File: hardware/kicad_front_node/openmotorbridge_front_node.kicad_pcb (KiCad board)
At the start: 2 copper layers, 68 x 44 mm, 32 parts, among them J1 12V_KL30_KL15_GND, J2 CAN_H_L_GND, J3 PTT_IN_GND, J4 USB_UPSTREAM_HOST, J5 USB_DN1_GLOVEBOX, J6 USB_DN2_CARPLAY, J7 USB-C_SERVICE, SW1 BOOT, SW2 RESET, U1 ESP32-C3-WROOM-02U, U2 USB2512B_AEC_HUB, U3 TPS2051B_CARPLAY_SWITCH, U4 TPS54302_BUCK_5V2A, U5 TCAN334G_CAN, U6 TLV75533P_3V3_500mA, Y1 24.000MHz

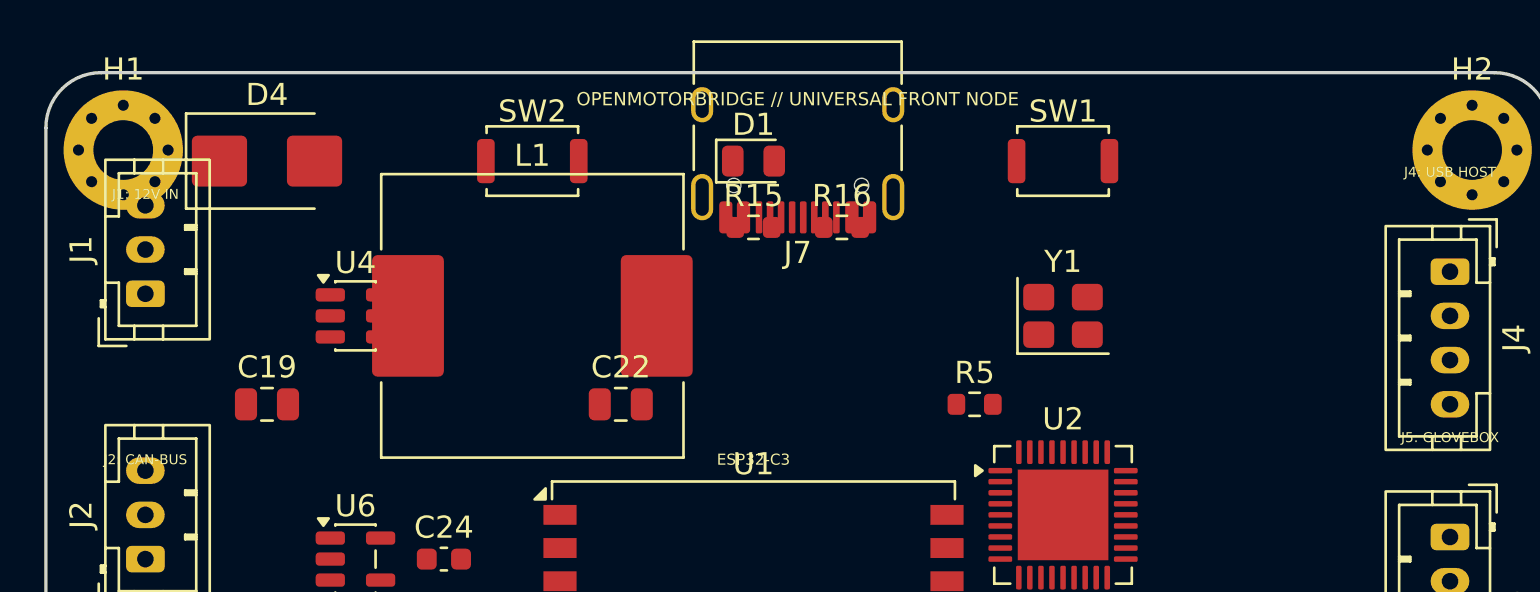
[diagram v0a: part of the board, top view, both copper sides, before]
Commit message: feat(hardware): upgrade front node power architecture to dual power (pure USB bus-powered default + optional switched 12V KL15)
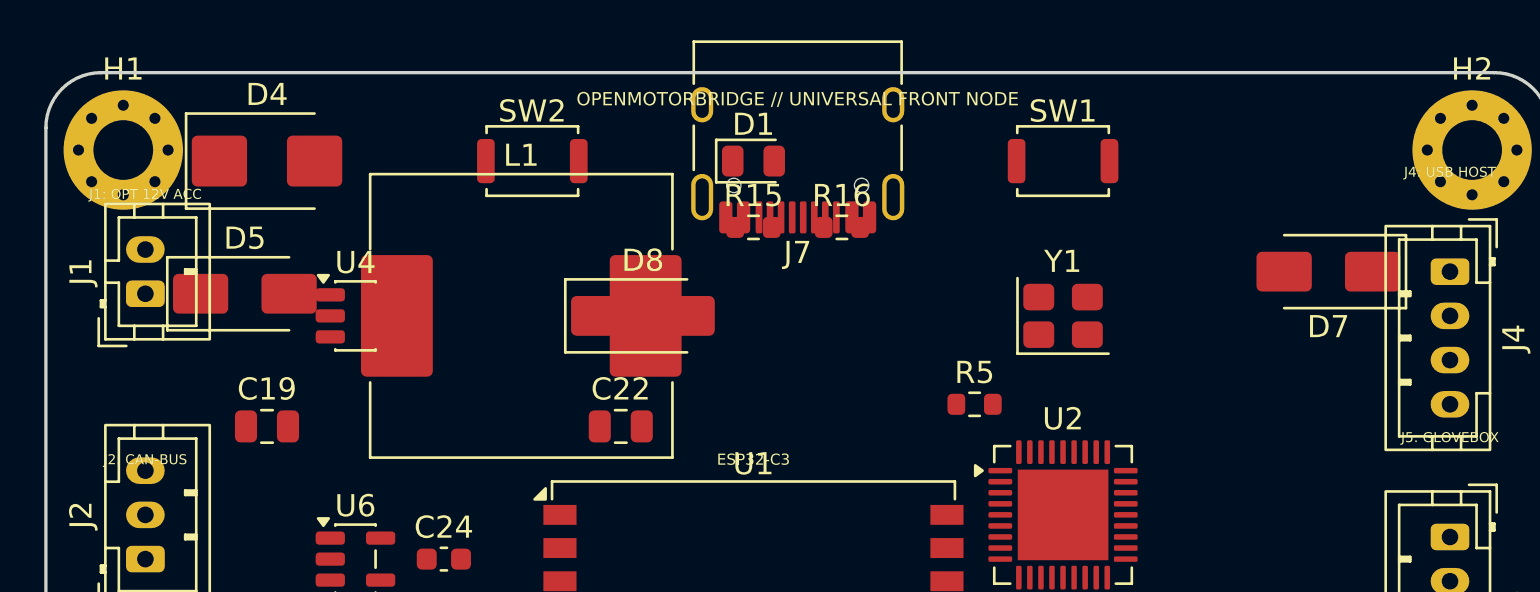
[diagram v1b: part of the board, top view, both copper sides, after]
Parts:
- added D5: SS34_REV_POL, D_SMA, F.Cu at (109.0, 80.0)
- added D7: SS34_USB_OR, D_SMA, F.Cu at (158.0, 79.0)
- added D8: SS34_BUCK_OR, D_SMA, F.Cu at (127.0, 81.0)
- J1: value 12V_KL30_KL15_GND -> OPT_12V_KL15_GND; footprint JST_PH_B3B-PH-K_1x03_P2.00mm_Vertical -> JST_PH_B2B-PH-K_1x02_P2.00mm_Vertical
- moved C19 1.00 mm to (110.0, 86.0)
- moved C22 1.00 mm to (126.0, 86.0)
- moved L1 0.50 mm to (121.5, 81.0)
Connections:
- C19 pad 1: KL30_12V -> VIN_BUCK
- D4 pad 1: KL30_12V -> VIN_BUCK
- J1 pad 1: KL30_12V -> KL15_12V_SW
- J1 pad 2: KL15_IGN -> GND
- L1 pad 2: VCC_5V -> VBUS_BUCK_OUT
- U4 pad 3: KL30_12V -> VIN_BUCK
- U4 pad 5: KL30_12V -> VIN_BUCK
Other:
- board text added: "J1: OPT 12V ACC"
- board text removed: "J1: 12V IN"

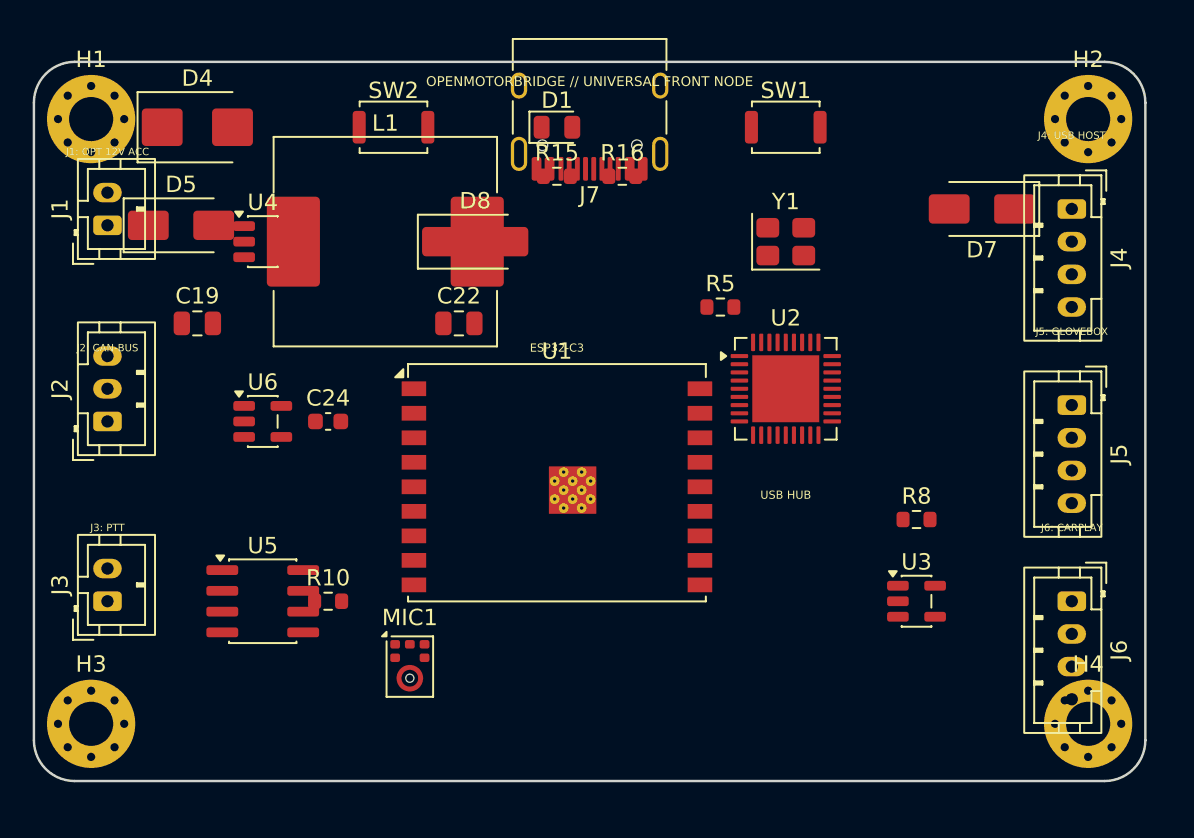
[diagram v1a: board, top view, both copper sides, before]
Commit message: fix(hardware): assign VCC_5V to overlapping USB-C pads A9 and B9 of J7 to eliminate 0.000mm clearance DRC lock
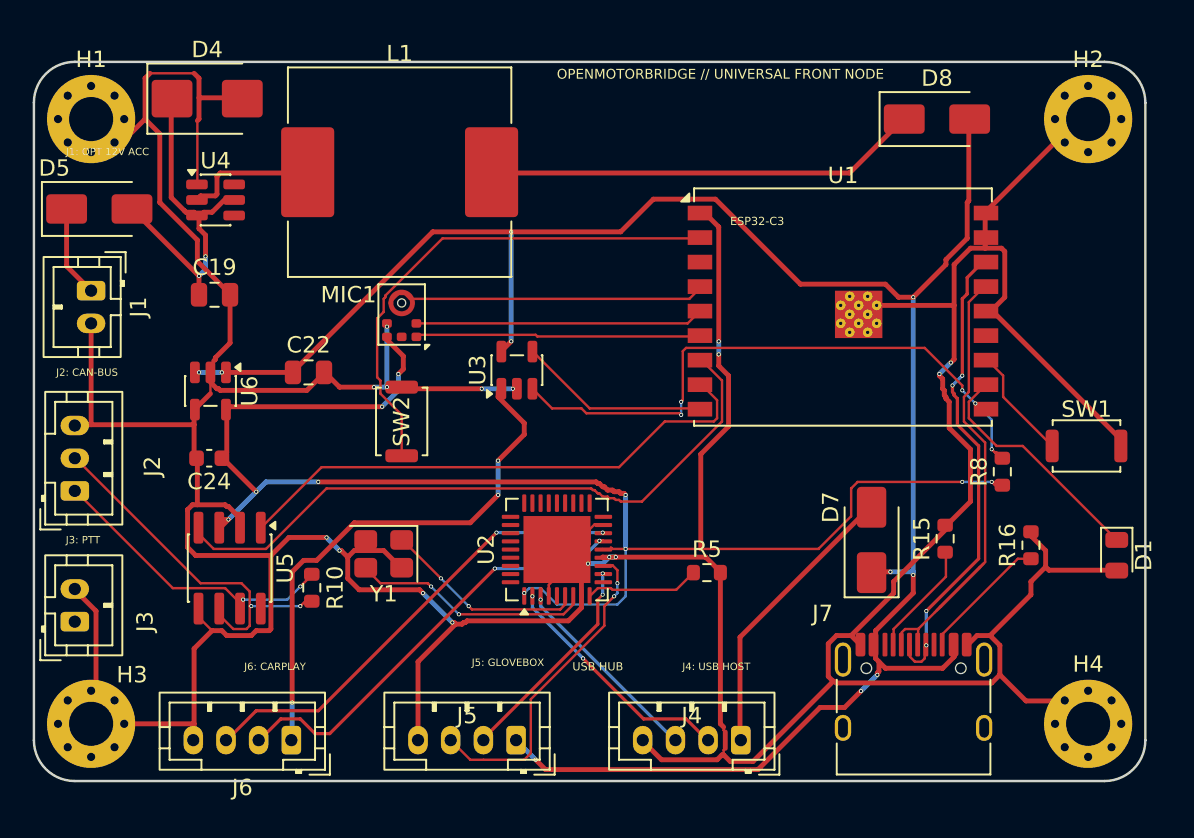
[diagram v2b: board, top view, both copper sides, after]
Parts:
- moved J6 48.5 mm to (115.8, 111.5), turned to 180 degrees
- moved D1 43.1 mm to (166.2, 100.2), turned to -90 degrees
- moved J7 42.2 mm to (153.8, 109.7), turned to 0 degrees
- moved J5 39.7 mm to (129.5, 111.5), turned to 180 degrees
- moved J4 38.3 mm to (143.2, 111.5), turned to 180 degrees
- moved R16 33.7 mm to (161.0, 99.6), turned to 90 degrees
- moved R15 32.5 mm to (155.8, 99.2), turned to 90 degrees
- moved Y1 31.1 mm to (121.4, 100.1), turned to 180 degrees
- moved D8 29.2 mm to (155.2, 73.5)
- moved U3 28.2 mm to (129.6, 88.9), turned to 90 degrees
- moved SW1 26.8 mm to (164.4, 93.5)
- moved MIC1 21.5 mm to (122.5, 85.5), turned to 180 degrees
- moved D7 21.3 mm to (151.2, 99.2), turned to 90 degrees
- moved U1 20.5 mm to (149.5, 85.2)
- moved SW2 18.0 mm to (122.5, 92.0), turned to 90 degrees
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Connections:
- J7 pad A5: (no net) -> USB_CC1
- J7 pad A9: (no net) -> VCC_5V
- J7 pad B5: (no net) -> USB_CC2
- J7 pad B9: (no net) -> VCC_5V
- R15 pad 1: (no net) -> USB_CC1
- R16 pad 1: (no net) -> USB_CC2
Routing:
- net GND: track 0.00 -> 302.2 mm, vias 0 -> 14
- net VCC_5V: track 0.00 -> 128.9 mm, vias 0 -> 10
- net VCC_3V3: track 0.00 -> 110.2 mm, vias 0 -> 12
- net TWAI_RX: track 0.00 -> 41.1 mm
- net OTTOCAST_FAULT_N: track 0.00 -> 38.2 mm, vias 0 -> 5
- net TWAI_TX: track 0.00 -> 33.2 mm
- net VCC_5V_OTTOCAST: track 0.00 -> 32.8 mm, vias 0 -> 3
- net ESP_EN: track 0.00 -> 31.4 mm
- net USB_SERV_DP: track 0.00 -> 29.1 mm, vias 0 -> 4
- net USB_DN2_DP: track 0.00 -> 28.3 mm, vias 0 -> 2
- net USB_DN2_DM: track 0.00 -> 26.9 mm, vias 0 -> 2
- net USB_SERV_DM: track 0.00 -> 26.8 mm
- net VBUS_BUCK_OUT: track 0.00 -> 26.7 mm
- net CAN_L: track 0.00 -> 22.9 mm, vias 0 -> 2
- net VIN_BUCK: track 0.00 -> 21.9 mm, vias 0 -> 2
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
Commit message: docs & feat: restructure Chapter 08 reference kits, update modular enclosures, front-node mechanics and firmware
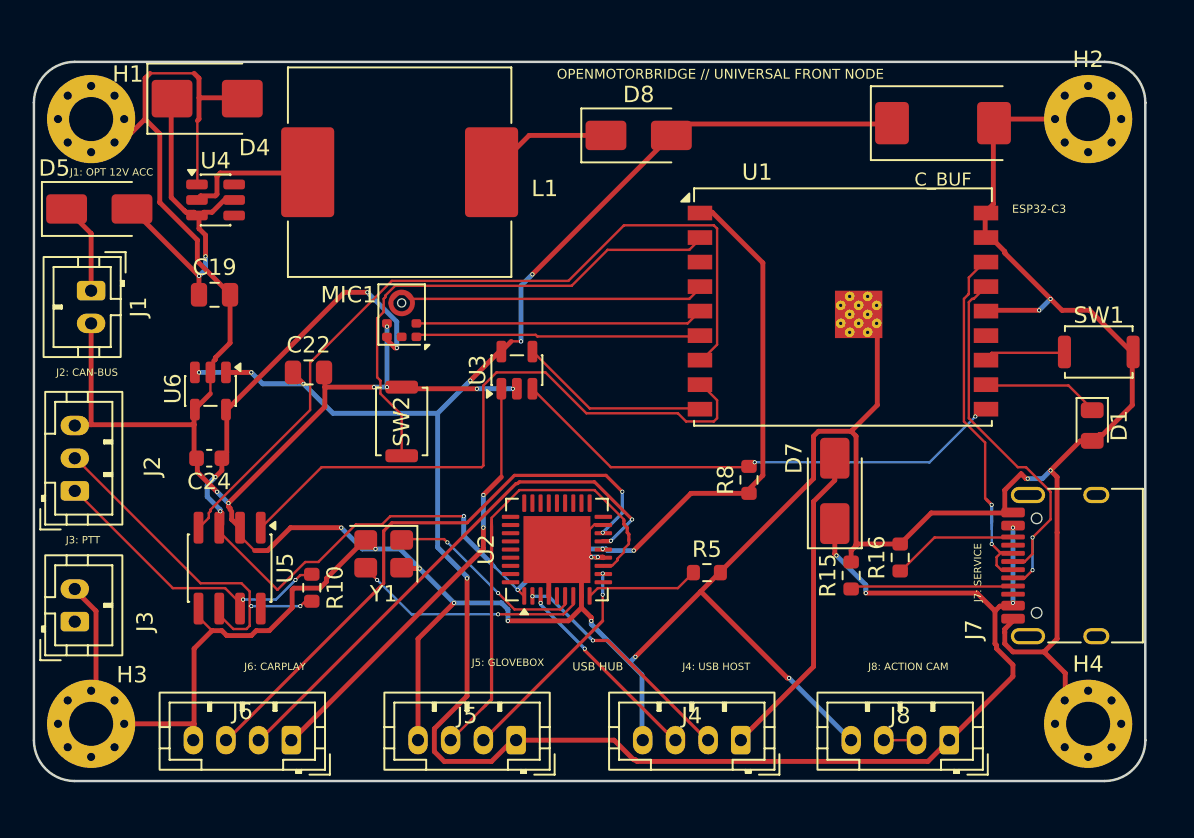
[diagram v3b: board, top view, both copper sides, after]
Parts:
- added C_BUF: 470uF_10V_POLYMER, CP_EIA-7343-31_Kemet-D, F.Cu at (155.6, 73.8)
- added J8: J8: ACTION_CAM_5V_PWR, JST_PH_B4B-PH-K_1x04_P2.00mm_Vertical, F.Cu at (156.0, 111.5)
- moved D8 18.3 mm to (137.0, 74.5)
- moved R8 15.5 mm to (143.8, 95.6)
- moved J7 13.5 mm to (163.9, 100.8), turned to 90 degrees
- moved D1 8.08 mm to (164.8, 92.2)
- moved R16 8.04 mm to (153.0, 100.3)
- moved R15 6.17 mm to (150.0, 101.4)
- moved SW1 5.80 mm to (165.2, 87.8)
- moved D7 3.75 mm to (149.0, 96.2)
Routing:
- net VCC_3V3: track 110.2 -> 86.6 mm, vias 12 -> 8
- net VBUS_BUCK_OUT: track 26.7 -> 8.00 mm
- net VCC_5V: track 128.9 -> 140.9 mm, vias 10 -> 11
- net TWAI_RX: track 41.1 -> 50.0 mm
- net USB_DN1_DP: track 20.0 -> 28.2 mm, vias 2 -> 0
- net USB_DN2_DP: track 28.3 -> 36.2 mm
- net LED_STATUS: track 14.6 -> 7.34 mm
- net USB_SERV_DP: track 29.1 -> 22.3 mm, vias 4 -> 2
- net OTTOCAST_FAULT_N: track 38.2 -> 31.3 mm, vias 5 -> 2
- net VCC_5V_OTTOCAST: track 32.8 -> 26.8 mm, vias 3 -> 2
- net USB_DN2_DM: track 26.9 -> 32.7 mm
- net TWAI_TX: track 33.2 -> 38.6 mm
- net USB_CC1: track 7.13 -> 10.0 mm
- net GND: track 302.2 -> 299.5 mm, vias 14 -> 21
- net USB_SERV_DM: track 26.8 -> 24.5 mm, vias 0 -> 2
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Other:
- board text added: "J7: SERVICE"
- board text added: "J8: ACTION CAM"
